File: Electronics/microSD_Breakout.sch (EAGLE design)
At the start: 2 parts, among them U1 USD-SOCKETUSD

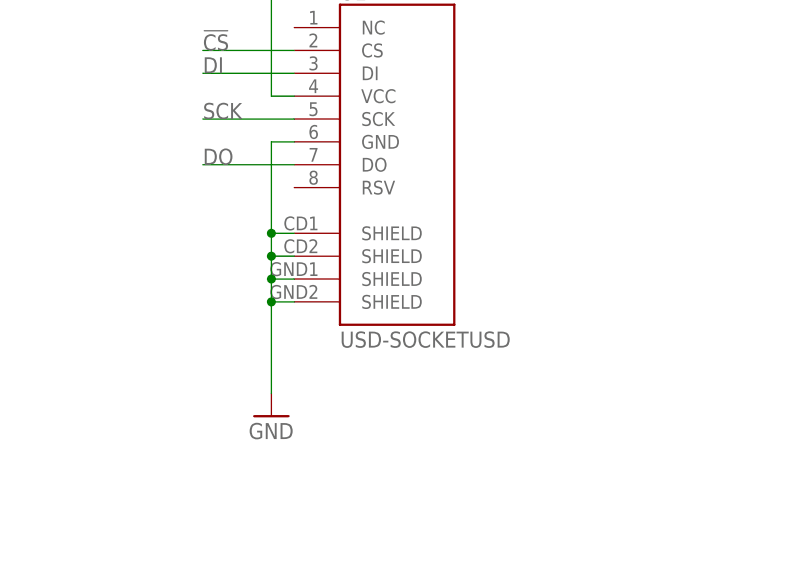
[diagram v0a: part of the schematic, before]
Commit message: Moved RC Mux to subdirectory. Minor changes to various other boards.
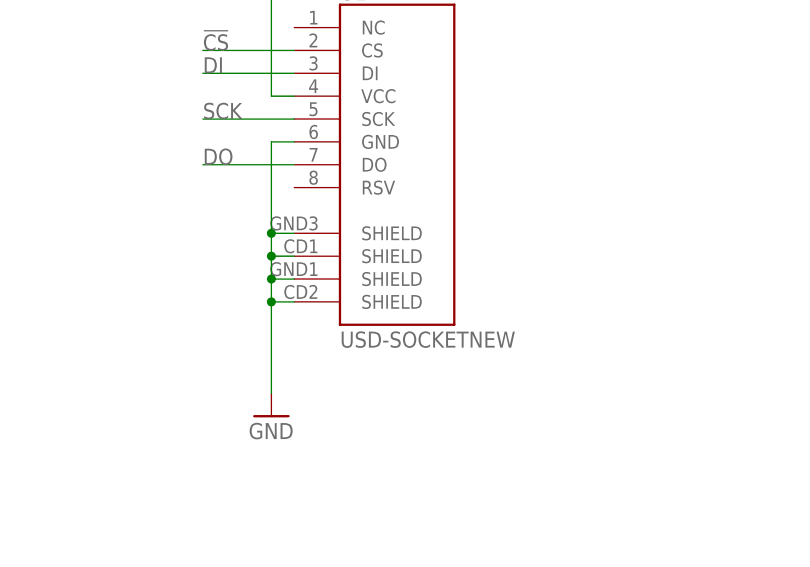
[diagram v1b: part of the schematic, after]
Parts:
- U1: value USD-SOCKETUSD -> USD-SOCKETNEW; device SparkFun:USD-SOCKETUSD -> SparkFun:USD-SOCKETNEW
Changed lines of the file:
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@@
 <grid distance="0.1" unitdist="inch" unit="inch" style="lines" multiple="1" display="no" altdistance="0.01" altunitdist="inch" altunit="inch"/>
 <layers>
-<layer number="1" name="Top" color="4" fill="1" visible="no" active="no"/>
-<layer number="16" name="Bottom" color="1" fill="1" visible="no" active="no"/>
-<layer number="17" name="Pads" color="2" fill="1" visible="no" active="no"/>
-<layer number="18" name="Vias" color="2" fill="1" visible="no" active="no"/>
-<layer number="19" name="Unrouted" color="6" fill="1" visible="no" active="no"/>
-<layer number="20" name="Dimension" color="15" fill="1" visible="no" active="no"/>
-<layer number="21" name="tPlace" color="7" fill="1" visible="no" active="no"/>
-<layer number="22" name="bPlace" color="7" fill="1" visible="no" active="no"/>
-<layer number="23" name="tOrigins" color="15" fill="1" visible="no" active="no"/>
-<layer number="24" name="bOrigins" color="15" fill="1" visible="no" active="no"/>
-<layer number="25" name="tNames" color="7" fill="1" visible="no" active="no"/>
-<layer number="26" name="bNames" color="7" fill="1" visible="no" active="no"/>
-<layer number="27" name="tValues" color="7" fill="1" visible="no" active="no"/>
-<layer number="28" name="bValues" color="7" fill="1" visible="no" active="no"/>
+<layer number="1" name="Top" color="4" fill="1" visible="yes" active="no"/>
+<layer number="16" name="Bottom" color="1" fill="1" visible="yes" active="no"/>
+<layer number="17" name="Pads" color="2" fill="1" visible="yes" active="no"/>
+<layer number="18" name="Vias" color="2" fill="1" visible="yes" active="no"/>
+<layer number="19" name="Unrouted" color="6" fill="1" visible="yes" active="no"/>
+<layer number="20" name="Dimension" color="15" fill="1" visible="yes" active="no"/>
+<layer number="21" name="tPlace" color="7" fill="1" visible="yes" active="no"/>
+<layer number="22" name="bPlace" color="7" fill="1" visible="yes" active="no"/>
+<layer number="23" name="tOrigins" color="15" fill="1" visible="yes" active="no"/>
+<layer number="24" name="bOrigins" color="15" fill="1" visible="yes" active="no"/>
+<layer number="25" name="tNames" color="7" fill="1" visible="yes" active="no"/>
+<layer number="26" name="bNames" color="7" fill="1" visible="yes" active="no"/>
+<layer number="27" name="tValues" color="7" fill="1" visible="yes" active="no"/>
+<layer number="28" name="bValues" color="7" fill="1" visible="yes" active="no"/>
 <layer number="29" name="tStop" color="7" fill="3" visible="no" active="no"/>
 <layer number="30" name="bStop" color="7" fill="6" visible="no" active="no"/>
@@
 <layer number="35" name="tGlue" color="7" fill="4" visible="no" active="no"/>
 <layer number="36" name="bGlue" color="7" fill="5" visible="no" active="no"/>
-<layer number="37" name="tTest" color="7" fill="1" visible="no" active="no"/>
-<layer number="38" name="bTest" color="7" fill="1" visible="no" active="no"/>
+<layer number="37" name="tTest" color="7" fill="1" visible="yes" active="no"/>
+<layer number="38" name="bTest" color="7" fill="1" visible="yes" active="no"/>
 <layer number="39" name="tKeepout" color="4" fill="11" visible="no" active="no"/>
 <layer number="40" name="bKeepout" color="1" fill="11" visible="no" active="no"/>
@@
 <layer number="44" name="Drills" color="7" fill="1" visible="no" active="no"/>
 <layer number="45" name="Holes" color="7" fill="1" visible="no" active="no"/>
-<layer number="46" name="Milling" color="3" fill="1" visible="no" active="no"/>
-<layer number="47" name="Measures" color="7" fill="1" visible="no" active="no"/>
-<layer number="48" name="Document" color="7" fill="1" visible="no" active="no"/>
-<layer number="49" name="Reference" color="7" fill="1" visible="no" active="no"/>
-<layer number="50" name="dxf" color="7" fill="1" visible="no" active="no"/>
-<layer number="51" name="tDocu" color="7" fill="1" visible="no" active="no"/>
-<layer number="52" name="bDocu" color="7" fill="1" visible="no" active="no"/>
-<layer number="53" name="tGND_GNDA" color="7" fill="9" visible="no" active="no"/>
-<layer number="54" name="bGND_GNDA" color="1" fill="9" visible="no" active="no"/>
-<layer number="56" name="wert" color="7" fill="1" visible="no" active="no"/>
+<layer number="46" name="Milling" color="3" fill="1" visible="yes" active="no"/>
+<layer number="47" name="Measures" color="7" fill="1" visible="yes" active="no"/>
+<layer number="48" name="Document" color="7" fill="1" visible="yes" active="no"/>
+<layer number="49" name="Reference" color="7" fill="1" visible="yes" active="no"/>
+<layer number="50" name="dxf" color="7" fill="1" visible="yes" active="no"/>
+<layer number="51" name="tDocu" color="7" fill="1" visible="yes" active="no"/>
+<layer number="52" name="bDocu" color="7" fill="1" visible="yes" active="no"/>
+<layer number="53" name="tGND_GNDA" color="7" fill="9" visible="yes" active="no"/>
+<layer number="54" name="bGND_GNDA" color="1" fill="9" visible="yes" active="no"/>
+<layer number="56" name="wert" color="7" fill="1" visible="yes" active="no"/>
 <layer number="91" name="Nets" color="2" fill="1" visible="yes" active="yes"/>
 <layer number="92" name="Busses" color="1" fill="1" visible="yes" active="yes"/>
@@
 </classes>
 <parts>
-<part name="U1" library="SparkFun" deviceset="USD-SOCKET" device="USD"/>
+<part name="U1" library="SparkFun" deviceset="USD-SOCKET" device="NEW"/>
 <part name="JP1" library="pinhead-2" deviceset="PINHD-2X03" device="_2.54"/>
 <part name="GND1" library="mes" deviceset="GND" device=""/>
